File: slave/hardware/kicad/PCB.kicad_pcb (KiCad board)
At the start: 4 copper layers, 223 parts, among them IC1 L6982C50, IC10 ESDALC6V1W5_SPLIT, IC11 ESDALC6V1W5_SPLIT, IC12 L9616, IC13 STM32G431C8T6TR, IC2 L6982C33, IC3 STEF12SGR, IC4 STEF12SGR, IC5 TSV772IST, IC6 TSV772IST, IC7 TSV772IST, IC9 TSV772IST, J2 AMPSEAL_8, J3 AMPSEAL_23, J4 USB_C_Receptacle_USB2.0_16P, Q1 IPD50P04P4L-11, Q2 BSS138, Q4 BSS138, SW1 SW_Push, SW2 SW_Push, U1 CH340C, Y1 8Mhz

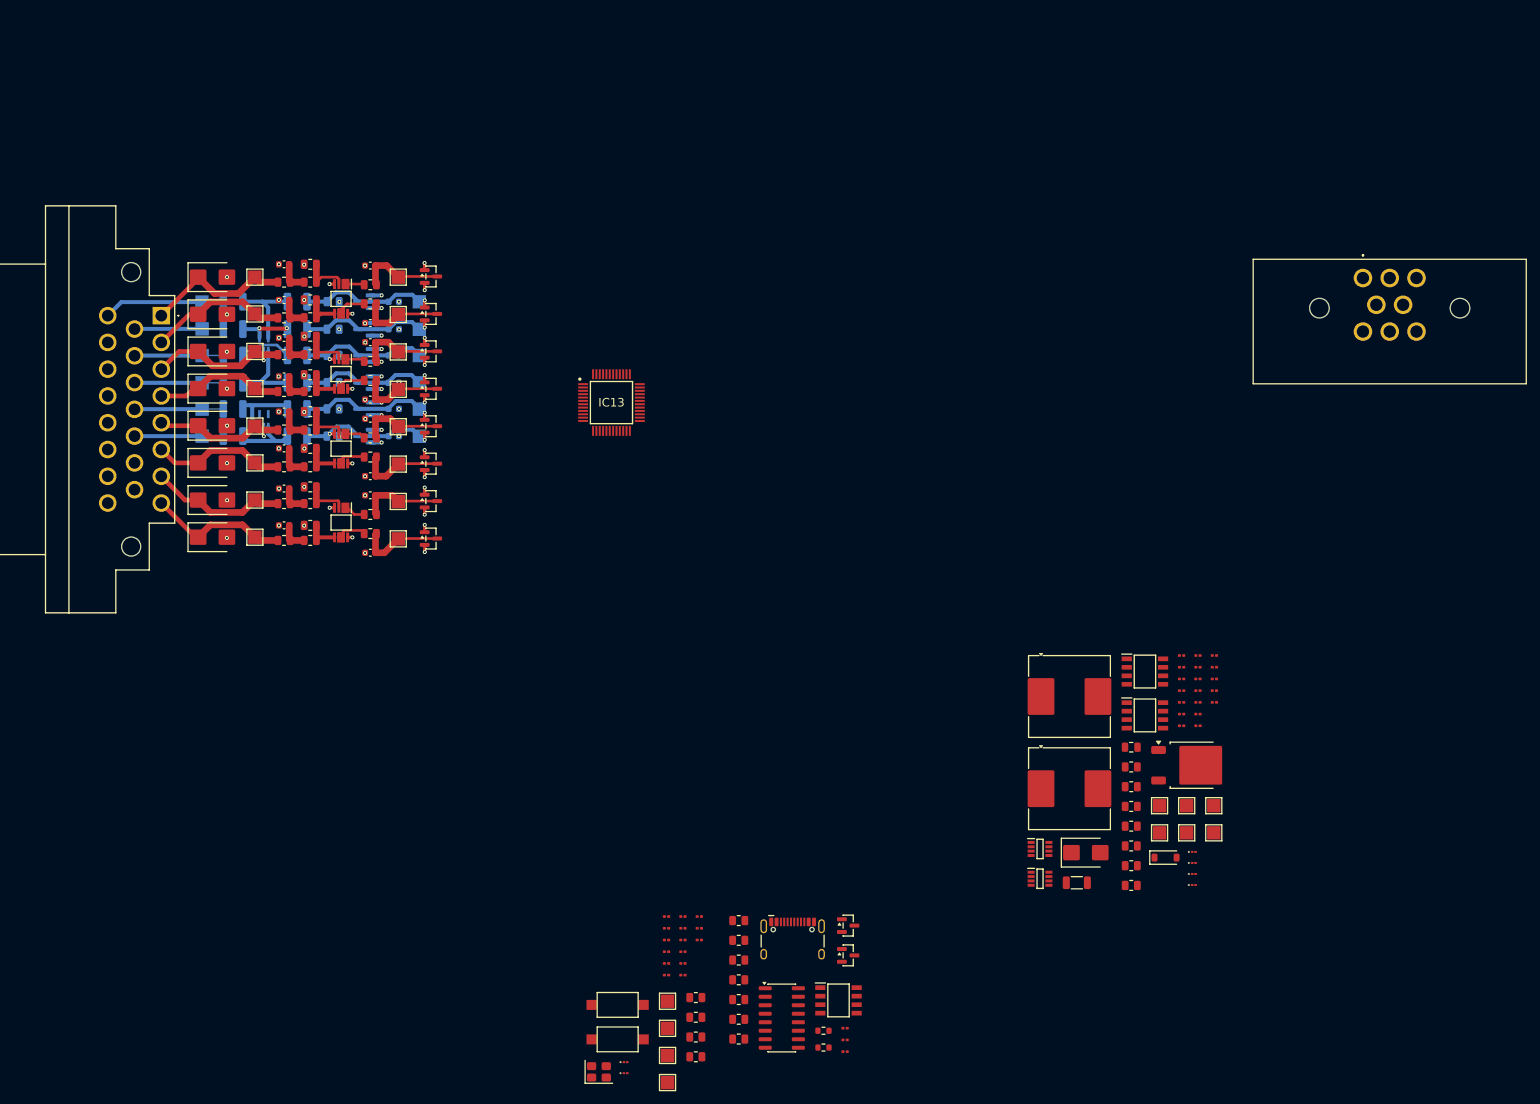
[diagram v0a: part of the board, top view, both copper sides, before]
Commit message: feat(HW): continue PCB layout and routing updates
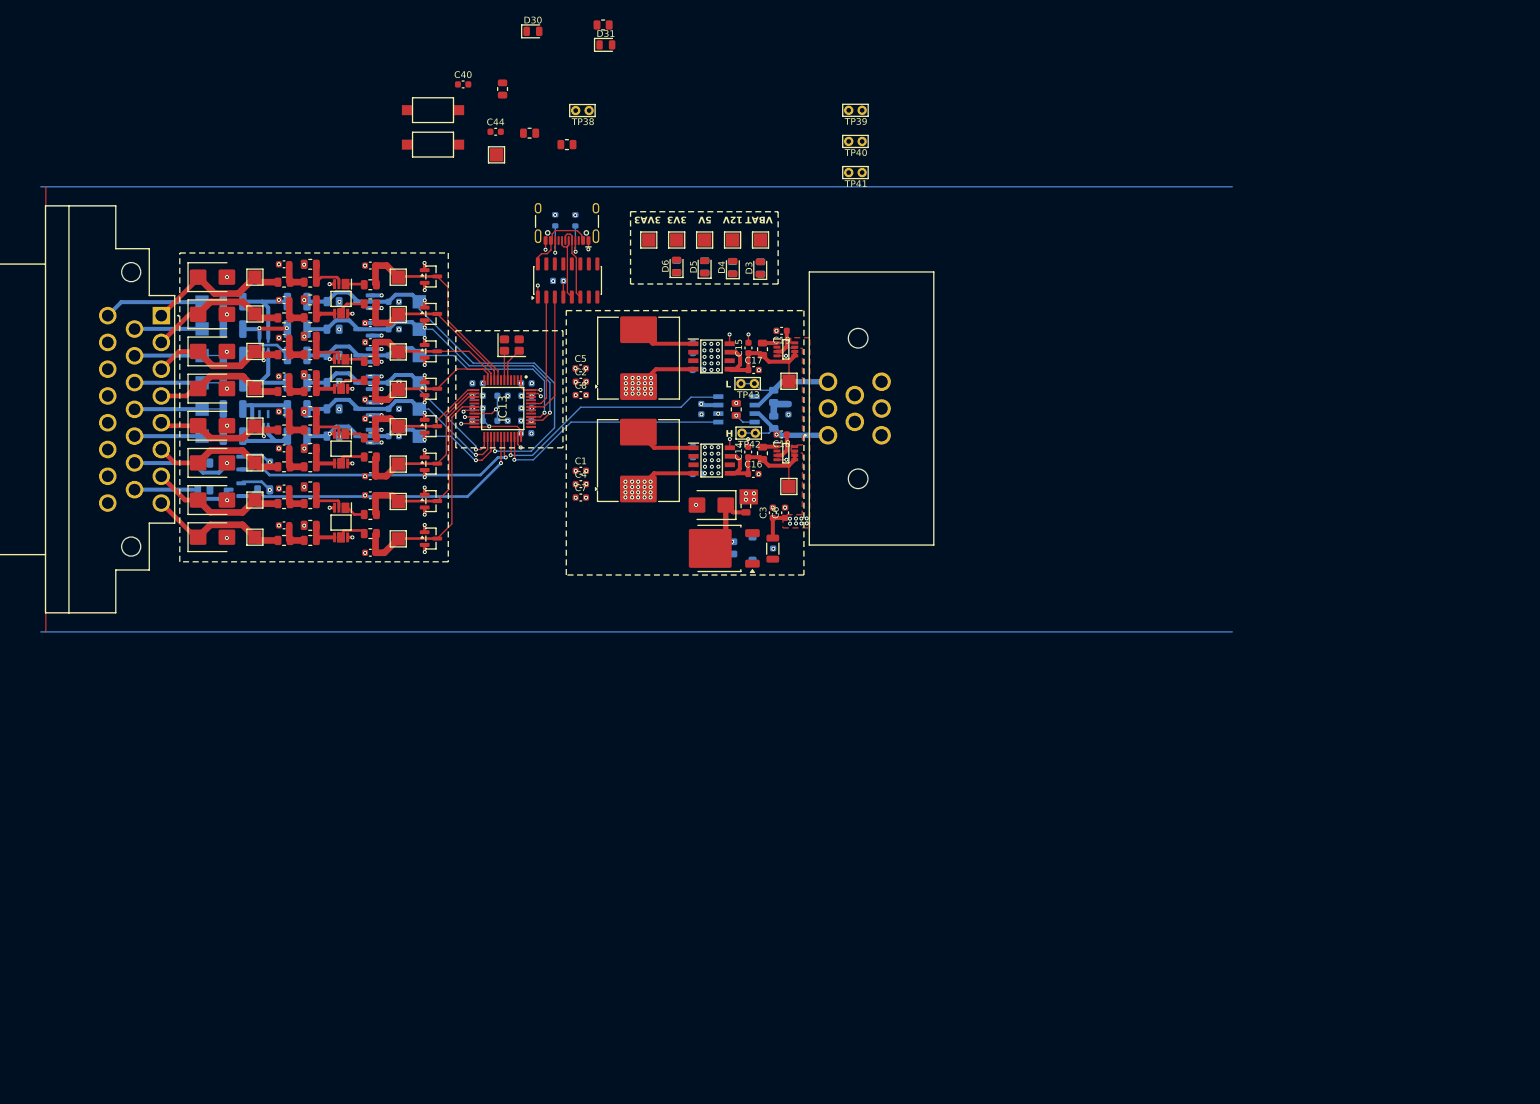
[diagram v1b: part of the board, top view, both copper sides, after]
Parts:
- removed TP23: ~, TestPoint:TestPoint_Pad_2.0x2.0mm
- added TP39: ~, TestPoint:TestPoint_Bridge_Pitch2.0mm_Drill0.7mm, F.Cu at (190.7, 40.6)
- added TP40: ~, TestPoint:TestPoint_Bridge_Pitch2.0mm_Drill0.7mm, F.Cu at (190.7, 45.2)
- added TP41: ~, TestPoint:TestPoint_Bridge_Pitch2.0mm_Drill0.7mm, F.Cu at (190.7, 49.9)
- added TP42: ~, TestPoint:TestPoint_Bridge_Pitch2.0mm_Drill0.7mm, F.Cu at (174.8, 88.8)
- added TP43: ~, TestPoint:TestPoint_Bridge_Pitch2.0mm_Drill0.7mm, F.Cu at (174.6, 81.4)
- C1, C14, C15, C16, C17, C18, C19, C2, C3, C4, C40, C44, C5, C6, C7, C8: footprint Capacitor_SMD:C_0201_0603Metric -> Capacitor_SMD:C_0603_1608Metric
- C10, C11, C12, C13, C36, C37, C38, C39, C41, C42, C43, C45, C46, C47, C48, C49, C56, C57, C58, C9, FB2: footprint Capacitor_SMD:C_0201_0603Metric -> Capacitor_SMD:C_0603_1608Metric; moved to B.Cu
- D1, IC12, Q2, Q4, R1, R4, R5, R6, R60, R61, R64, R65, R69, R7, R70, R71, R73: moved to B.Cu
- D3, D30, D31, D4, D5, D6: footprint LED_SMD:LED_01005_0402Metric -> LED_SMD:LED_0805_2012Metric
- TP38: footprint TestPoint:TestPoint_Pad_2.0x2.0mm -> TestPoint:TestPoint_Bridge_Pitch2.0mm_Drill0.7mm
- moved R66 154.8 mm to (154.0, 27.8)
- moved D30 154.6 mm to (143.5, 28.8)
- moved D31 153.7 mm to (154.4, 30.8)
- moved TP38 145.9 mm to (149.9, 40.6)
- moved R40 138.8 mm to (139.0, 37.4), turned to -90 degrees
- moved SW1 136.5 mm to (128.6, 40.5)
- moved SW2 136.5 mm to (128.6, 45.7)
- moved C40 134.8 mm to (133.1, 36.7)
- moved R63 134.7 mm to (148.6, 45.7)
- moved R41 134.4 mm to (143.0, 44.0)
- moved TP24 133.0 mm to (138.1, 47.2)
- moved R73 129.0 mm to (149.9, 57.0), turned to -90 degrees
- moved R71 127.5 mm to (146.9, 57.0), turned to -90 degrees
- moved C44 123.9 mm to (137.9, 43.8)
- moved C58 122.9 mm to (147.3, 66.1)
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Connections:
- IC13 pad 39: MCU_HS_02 -> MCU_HS_01
- IC13 pad 40: MCU_HS_01 -> MCU_HS_02
- J2 pad 3: VBAT -> CAN_L
- J2 pad 5: CAN_L -> VBAT
- TP4 pad 1: Net-(D2-K) -> VBAT
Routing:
- net SDA01_3V3: track 0.00 -> 45.7 mm, vias 0 -> 1
- net MCU_LS_04: track 18.8 -> 63.9 mm, vias 0 -> 1
- net SCL01_3V3: track 0.00 -> 44.9 mm, vias 0 -> 1
- net +3.3V: track 9.80 -> 51.7 mm, vias 6 -> 39
- net CAN_RX: track 0.00 -> 37.5 mm, vias 0 -> 1
- net CAN_TX: track 0.00 -> 36.3 mm, vias 0 -> 1
- net MCU_HS_01: track 18.8 -> 49.4 mm, vias 0 -> 1
- net MCU_HS_02: track 18.8 -> 46.1 mm, vias 0 -> 1
- net +5V: track 0.00 -> 26.6 mm, vias 0 -> 24
- net ADC2_OUT3: track 13.0 -> 36.0 mm
- net Net-(IC1-EN/CLKIN): track 0.00 -> 21.6 mm
- net Net-(IC2-EN/CLKIN): track 0.00 -> 20.7 mm
- net ADC1_OUT0: track 12.9 -> 32.6 mm
- net GNDREF: track 24.2 -> 43.6 mm, vias 64 -> 141
- net UART_TX: track 0.00 -> 19.0 mm
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- added copper zone on F.Cu, net +12V
- added copper zone on In2.Cu, net +12V
- added copper zone on In2.Cu, net +3.3V
- added copper zone on In2.Cu, net +3.3VA
- added copper zone on In2.Cu, net +5V
- added copper zone on In1.Cu, net GNDREF
- added copper zone on In2.Cu, net VBAT
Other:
- board text added: "12V"
- board text added: "3V3"
- board text added: "3VA3"
- board text added: "5V"
- board text added: "H"
- board text added: "L"
- board text added: "VBAT"
